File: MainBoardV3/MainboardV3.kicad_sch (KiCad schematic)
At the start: 32 parts, among them J1 Conn_01x02, J10 Conn_01x04, J11 Conn_01x02, J18 Conn_01x03, J19 Conn_02x03_Odd_Even, J2 Conn_01x04, J20 Conn_02x03_Odd_Even, J21 Conn_02x03_Odd_Even, J22 Conn_01x03, J23 Conn_01x05, J24 Conn_02x05_Odd_Even, J3 Conn_01x03, J4 Conn_01x04, J5 Conn_01x05, J7 Conn_01x04, J8 Conn_01x04, J9 Conn_01x04, U2 ESP32-S3-DevKitC

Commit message: Modified to suit needs
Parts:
- removed A1, A2, A3: Pololu_Breakout_DRV8825, Module:Pololu_Breakout-16_15.2x20.3mm, symbol Driver_Motor:Pololu_Breakout_DRV8825
- removed C7, C8, C9: C_Polarized, Capacitor_THT:CP_Radial_D8.0mm_P3.50mm, symbol Device:C_Polarized
- removed J10, J2, J4: Conn_01x04, Connector_Molex:Molex_KK-254_AE-6410-04A_1x04_P2.54mm_Vertical, symbol Connector_Generic:Conn_01x04
- removed J18: Conn_01x03, Connector_PinHeader_2.54mm:PinHeader_1x03_P2.54mm_Vertical, symbol Connector_Generic:Conn_01x03
- removed J19, J20, J21: Conn_02x03_Odd_Even, Connector_PinHeader_2.54mm:PinHeader_2x03_P2.54mm_Vertical, symbol Connector_Generic:Conn_02x03_Odd_Even
- removed J5: Conn_01x05, Connector_JST:JST_XH_B5B-XH-A_1x05_P2.50mm_Vertical, symbol Connector_Generic:Conn_01x05
- removed J7, J8, J9: Conn_01x04, Connector_JST:JST_XH_B4B-XH-A_1x04_P2.50mm_Vertical, symbol Connector_Generic:Conn_01x04
- added C1, C2, C3: C_Polarized, Capacitor_THT:CP_Radial_D8.0mm_P3.50mm, symbol Device:C_Polarized
- added Conn12V1: Conn12V, Connector_AMASS:AMASS_XT30U-F_1x02_P5.0mm_Vertical, symbol Connector_Generic:Conn_01x02
- added Conn5V1: Conn5V, Connector_Molex:Molex_KK-254_AE-6410-02A_1x02_P2.54mm_Vertical, symbol Connector_Generic:Conn_01x02
- added Conn5VL1: Conn5VL, Connector_Molex:Molex_KK-254_AE-6410-02A_1x02_P2.54mm_Vertical, symbol Connector_Generic:Conn_01x02
- added Conn5VP1: Conn5VP, Connector_Molex:Molex_KK-396_A-41791-0002_1x02_P3.96mm_Vertical, symbol Connector_Generic:Conn_01x02
- added ConnAffOled1, ConnAffOled2: ConnAffOled, Connector_JST:JST_EH_B6B-EH-A_1x06_P2.50mm_Vertical, symbol Connector_Generic:Conn_01x06
- added ConnBATT1: ConnBATT, Connector_AMASS:AMASS_XT60-F_1x02_P7.20mm_Vertical, symbol Connector_Generic:Conn_01x02
- added ConnIFM_1: ConnIFM_1, Connector_Molex:Molex_KK-254_AE-6410-03A_1x03_P2.54mm_Vertical, symbol Connector_Generic:Conn_01x03
- added ConnIFM_2: ConnIFM_2, Connector_Molex:Molex_KK-254_AE-6410-03A_1x03_P2.54mm_Vertical, symbol Connector_Generic:Conn_01x03
- added ConnIFM_3: ConnIFM_3, Connector_Molex:Molex_KK-254_AE-6410-03A_1x03_P2.54mm_Vertical, symbol Connector_Generic:Conn_01x03
- added ConnMotor1: ConnMotor1, Connector_JST:JST_EH_B6B-EH-A_1x06_P2.50mm_Vertical, symbol Connector_Generic:Conn_01x06
- added ConnMotor2: ConnMotor2, Connector_JST:JST_EH_B6B-EH-A_1x06_P2.50mm_Vertical, symbol Connector_Generic:Conn_01x06
- added ConnMotor3: ConnMotor3, Connector_JST:JST_EH_B6B-EH-A_1x06_P2.50mm_Vertical, symbol Connector_Generic:Conn_01x06
- added ConnPCA1: Conn_01x06, Connector_JST:JST_EH_B6B-EH-A_1x06_P2.50mm_Vertical, symbol Connector_Generic:Conn_01x06
- added Conn_LIDAR1, Conn_LIDAR2: Conn_LIDAR, Connector_JST:JST_EH_B5B-EH-A_1x05_P2.50mm_Vertical, symbol Connector_Generic:Conn_01x05
- added R10, R6, R8: 470, Resistor_SMD:R_1206_3216Metric_Pad1.30x1.75mm_HandSolder, symbol Device:R_Small
- added R11, R7, R9: 110, Resistor_SMD:R_1206_3216Metric_Pad1.30x1.75mm_HandSolder, symbol Device:R_Small
- Tir.1: footprint Connector_JST:JST_XH_B2B-XH-A_1x02_P2.50mm_Vertical -> Connector_Molex:Molex_KK-254_AE-6410-02A_1x02_P2.54mm_Vertical
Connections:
- net +12V: now also Conn12V1.2 (Pin_2), ConnIFM_1.2 (Pin_2), ConnIFM_2.2 (Pin_2), ConnIFM_3.2 (Pin_2)
- net +3.3V: no longer U2.1 (3V3), U2.2 (3V3)
- net +5V: now also Conn5V1.1 (Pin_1), ConnPCA1.5 (Pin_5)
- net +5VP: now also Conn5VP1.1 (Pin_1), ConnPCA1.6 (Pin_6)
- net DIR1: now also ConnMotor1.6 (Pin_6)
- net DIR2: now also ConnMotor2.6 (Pin_6)
- net DIR3: now also ConnMotor3.6 (Pin_6)
- net EN: now also ConnMotor2.4 (Pin_4), ConnMotor3.4 (Pin_4)
- net GND: now also C1.2, C2.2, C3.2, Conn12V1.1 (Pin_1), Conn5V1.2 (Pin_2), Conn5VL1.2 (Pin_2), Conn5VP1.2 (Pin_2), ConnAffOled1.1 (Pin_1), ConnAffOled1.3 (Pin_3), ConnAffOled2.1 (Pin_1), ConnAffOled2.3 (Pin_3), ConnBATT1.1 (Pin_1), ConnIFM_1.3 (Pin_3), ConnIFM_2.3 (Pin_3), ConnIFM_3.3 (Pin_3), ConnMotor1.2 (Pin_2), ConnMotor2.2 (Pin_2), ConnMotor3.2 (Pin_2), ConnPCA1.1 (Pin_1), Conn_LIDAR1.2 (Pin_2), Conn_LIDAR2.2 (Pin_2), R11.2, R7.2, R9.2
- net LIDARRX: now also Conn_LIDAR1.3 (Pin_3), Conn_LIDAR2.3 (Pin_3)
- net LIDARTX: now also Conn_LIDAR1.4 (Pin_4), Conn_LIDAR2.4 (Pin_4)
- net PWMLIDAR: now also Conn_LIDAR1.1 (Pin_1), Conn_LIDAR2.1 (Pin_1)
- net SCL: now also ConnAffOled1.4 (Pin_4), ConnAffOled2.4 (Pin_4), ConnPCA1.3 (Pin_3)
- net SDA: now also ConnAffOled1.5 (Pin_5), ConnAffOled2.5 (Pin_5), ConnPCA1.4 (Pin_4)
- net STEP1: now also ConnMotor1.5 (Pin_5)
- net STEP2: now also ConnMotor2.5 (Pin_5)
- net STEP3: now also ConnMotor3.5 (Pin_5)
- new net: U2.1 (3V3), U2.2 (3V3)
- new net: ConnIFM_3.1 (Pin_1), R10.1
- new net: ConnIFM_1.1 (Pin_1), R6.1
- new net: ConnIFM_2.1 (Pin_1), R8.1
- new net +5VL: Conn5VL1.1 (Pin_1), ConnAffOled1.2 (Pin_2), ConnAffOled2.2 (Pin_2), Conn_LIDAR1.5 (Pin_5), Conn_LIDAR2.5 (Pin_5)
- new net +BATT: C1.1, C2.1, C3.1, ConnBATT1.2 (Pin_2), ConnMotor1.1 (Pin_1), ConnMotor2.1 (Pin_1), ConnMotor3.1 (Pin_1)
- new net ENA_STEPPERS: ConnMotor1.4 (Pin_4)
- new net IFM1: R6.2, R7.1
- new net IFM2: R8.2, R9.1
- new net IFM3: R10.2, R11.1
- new net RESET_OLED: ConnAffOled1.6 (Pin_6), ConnAffOled2.6 (Pin_6)
- new net SERVO_ENABLE: ConnPCA1.2 (Pin_2)
- no-connect marks 8 -> 5
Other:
- note added: "Alimentation 5V Logique"
- note added: "Alimentation 5V Puissance"
- note added: "Vout = 2,276V"
- moved on the sheet: H4, U5

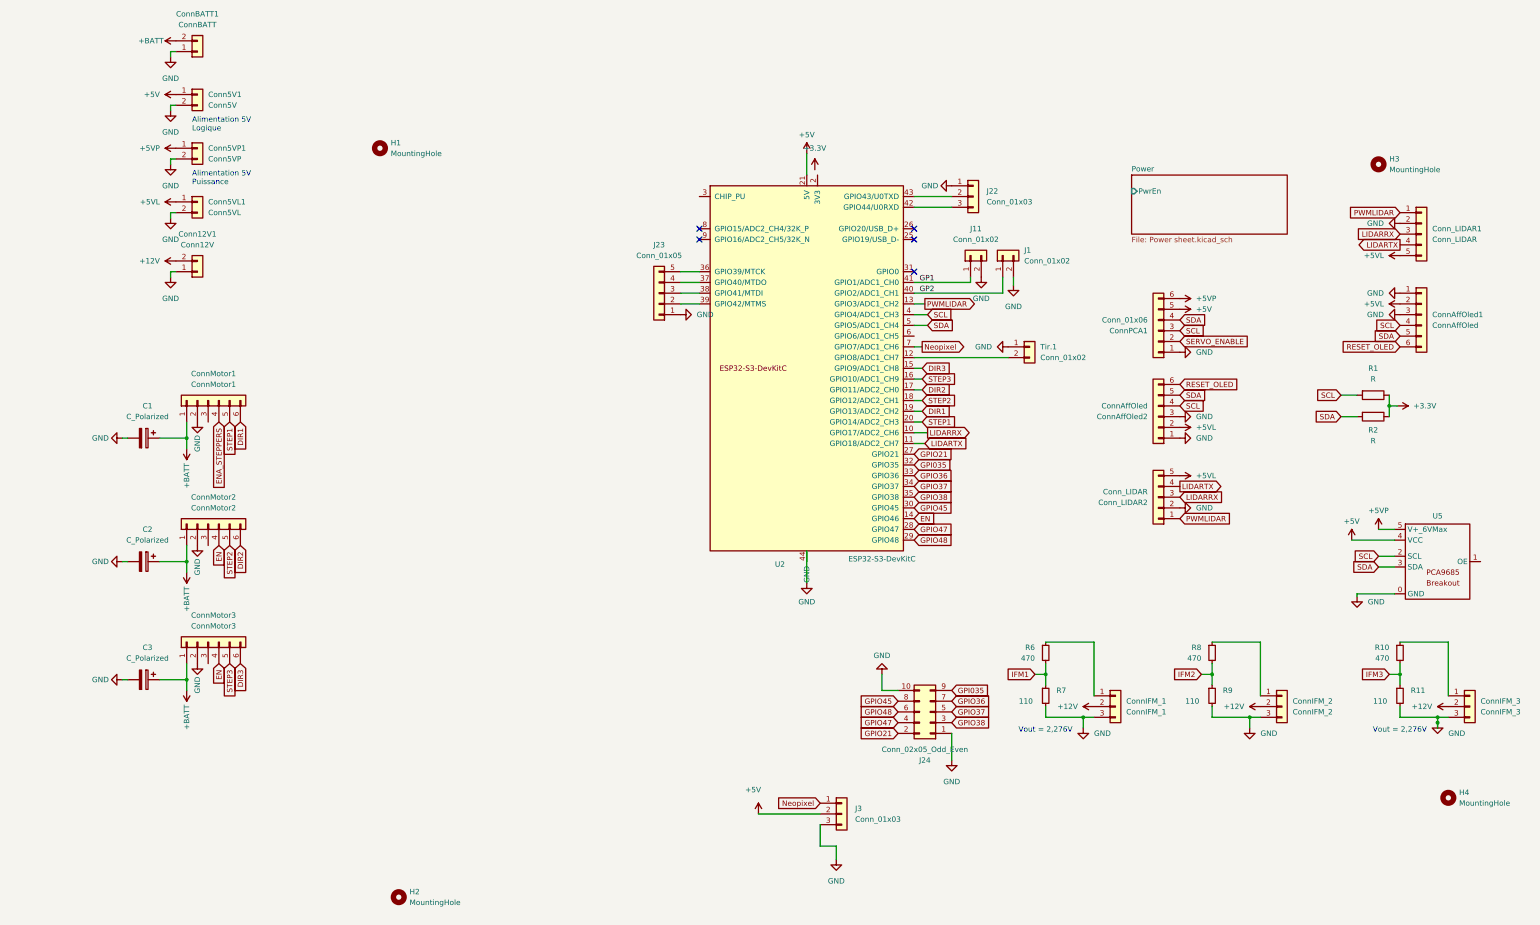
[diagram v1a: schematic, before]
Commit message: Adapted schematic to existing needs
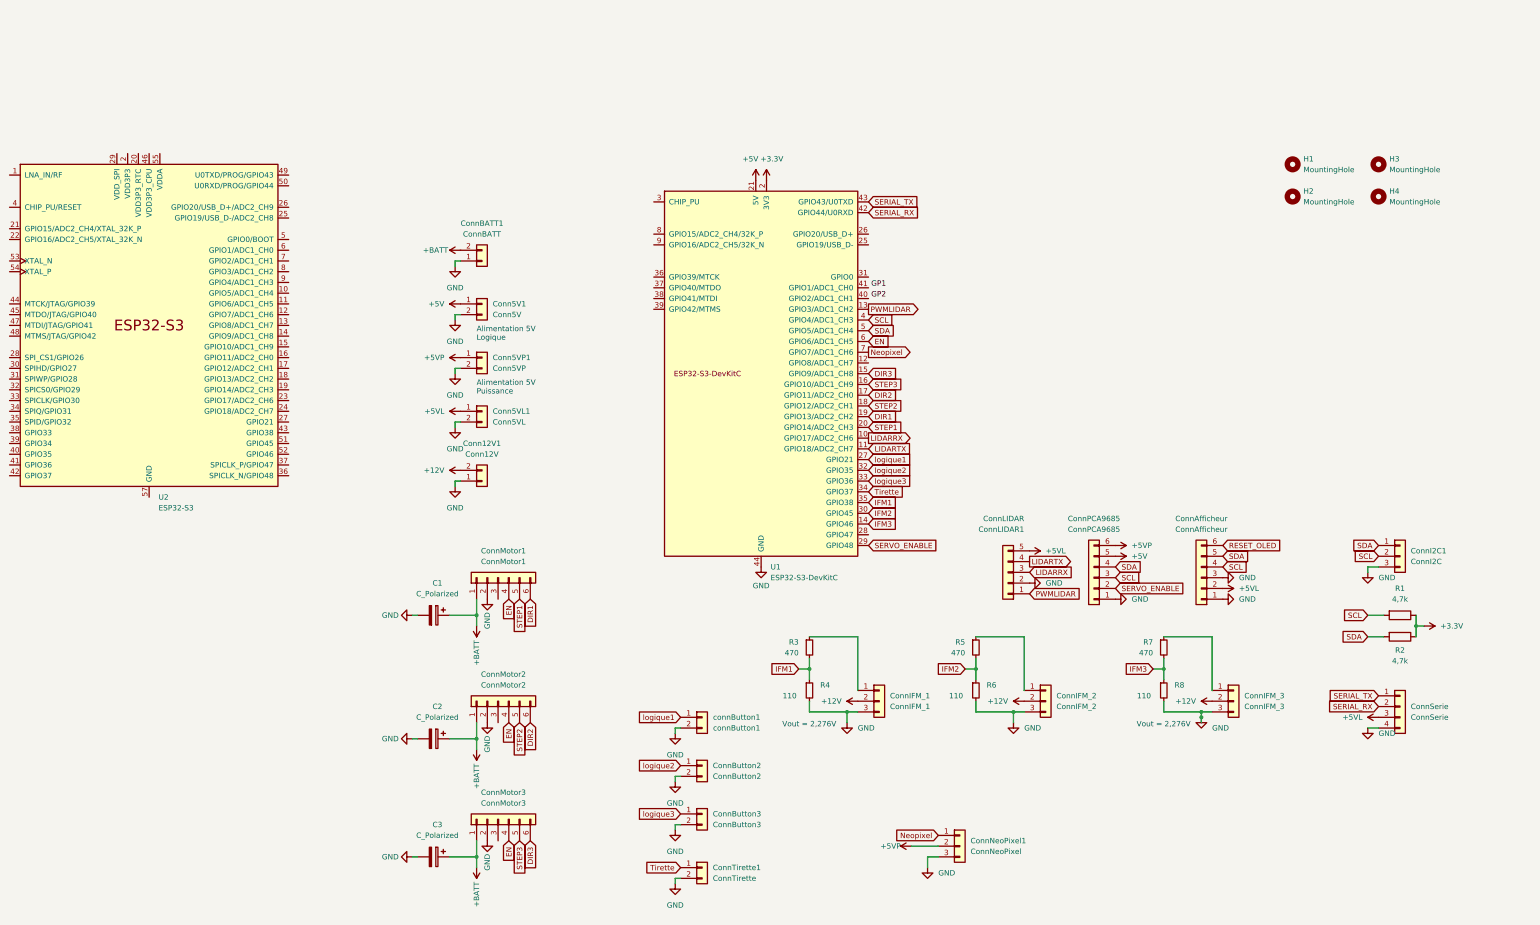
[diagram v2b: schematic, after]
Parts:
- removed ConnAffOled1: ConnAffOled, Connector_JST:JST_EH_B6B-EH-A_1x06_P2.50mm_Vertical, symbol Connector_Generic:Conn_01x06
- removed Conn_LIDAR1: Conn_LIDAR, Connector_JST:JST_EH_B5B-EH-A_1x05_P2.50mm_Vertical, symbol Connector_Generic:Conn_01x05
- removed J1, J11: Conn_01x02, Connector_JST:JST_XH_B2B-XH-A_1x02_P2.50mm_Vertical, symbol Connector_Generic:Conn_01x02
- removed J22, J3: Conn_01x03, Connector_PinHeader_2.54mm:PinHeader_1x03_P2.54mm_Vertical, symbol Connector_Generic:Conn_01x03
- removed J23: Conn_01x05, Connector_JST:JST_XH_B5B-XH-A_1x05_P2.50mm_Vertical, symbol Connector_Generic:Conn_01x05
- removed J24: Conn_02x05_Odd_Even, Connector_IDC:IDC-Header_2x05_P2.54mm_Vertical, symbol Connector_Generic:Conn_02x05_Odd_Even
- removed Tir.1: Conn_01x02, Connector_Molex:Molex_KK-254_AE-6410-02A_1x02_P2.54mm_Vertical, symbol Connector_Generic:Conn_01x02
- removed U2: ESP32-S3-DevKitC, ESP:ESP32-S3-DevKitC, symbol ESP32:ESP32-S3-DevKitC
- removed U5: ~, Custom:PCA9685breakout, symbol PCM:PWMI2C
- added ConnButton2: ConnButton2, Connector_Molex:Molex_KK-254_AE-6410-02A_1x02_P2.54mm_Vertical, symbol Connector_Generic:Conn_01x02
- added ConnButton3: ConnButton3, Connector_Molex:Molex_KK-254_AE-6410-02A_1x02_P2.54mm_Vertical, symbol Connector_Generic:Conn_01x02
- added ConnI2C1: ConnI2C, Connector_Molex:Molex_KK-254_AE-6410-03A_1x03_P2.54mm_Vertical, symbol Connector_Generic:Conn_01x03
- added ConnNeoPixel1: ConnNeoPixel, Connector_Molex:Molex_KK-254_AE-6410-03A_1x03_P2.54mm_Vertical, symbol Connector_Generic:Conn_01x03
- added ConnSerie: ConnSerie, Connector_JST:JST_EH_B4B-EH-A_1x04_P2.50mm_Vertical, symbol Connector_Generic:Conn_01x04
- added ConnTirette1: ConnTirette, Connector_Molex:Molex_KK-254_AE-6410-02A_1x02_P2.54mm_Vertical, symbol Connector_Generic:Conn_01x02
- added U1: ESP32-S3-DevKitC, PCM_Espressif:ESP32-S3-DevKitC, symbol PCM_Espressif:ESP32-S3-DevKitC
- added U2: ESP32-S3, Package_DFN_QFN:QFN-56-1EP_7x7mm_P0.4mm_EP5.6x5.6mm, symbol PCM_Espressif:ESP32-S3
- added connButton1: connButton1, Connector_Molex:Molex_KK-254_AE-6410-02A_1x02_P2.54mm_Vertical, symbol Connector_Generic:Conn_01x02
- ConnAfficheur: renamed from ConnAffOled2; value ConnAffOled -> ConnAfficheur
- ConnLIDAR1: renamed from Conn_LIDAR2; value Conn_LIDAR -> ConnLIDAR
- ConnPCA9685: renamed from ConnPCA1; value Conn_01x06 -> ConnPCA9685
- R1, R2: value R -> 4,7k
- renumbered R6 to R3, R7 to R4, R8 to R5, R9 to R6, R10 to R7, R11 to R8
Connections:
- net ENA_STEPPERS is gone; now on net EN: ConnMotor1.4 (Pin_4)
- net +3.3V: now also U1.1 (3V3), U1.2 (3V3)
- net +5V: now also U1.21 (5V)
- net +5VL: now also ConnSerie.3 (Pin_3)
- net +5VP: now also ConnNeoPixel1.2 (Pin_2)
- net DIR1: now also U1.19 (GPIO13/ADC2_CH2)
- net DIR2: now also U1.17 (GPIO11/ADC2_CH0)
- net DIR3: now also U1.15 (GPIO9/ADC1_CH8)
- net EN: now also U1.6 (GPIO6/ADC1_CH5)
- net GND: now also ConnButton2.2 (Pin_2), ConnButton3.2 (Pin_2), ConnI2C1.3 (Pin_3), ConnNeoPixel1.3 (Pin_3), ConnSerie.4 (Pin_4), ConnTirette1.2 (Pin_2), U1.22 (GND), U1.23 (GND), U1.24 (GND), U1.44 (GND), connButton1.2 (Pin_2)
- net IFM1: now also U1.35 (GPIO38)
- net IFM2: now also U1.30 (GPIO45)
- net IFM3: now also U1.14 (GPIO46)
- net LIDARRX: now also U1.10 (GPIO17/ADC2_CH6)
- net LIDARTX: now also U1.11 (GPIO18/ADC2_CH7)
- net Neopixel: now also ConnNeoPixel1.1 (Pin_1), U1.7 (GPIO7/ADC1_CH6)
- net PWMLIDAR: now also U1.13 (GPIO3/ADC1_CH2)
- net SCL: now also ConnI2C1.2 (Pin_2), U1.4 (GPIO4/ADC1_CH3)
- net SDA: now also ConnI2C1.1 (Pin_1), U1.5 (GPIO5/ADC1_CH4)
- net SERVO_ENABLE: now also U1.29 (GPIO48)
- net STEP1: now also U1.20 (GPIO14/ADC2_CH3)
- net STEP2: now also U1.18 (GPIO12/ADC2_CH1)
- net STEP3: now also U1.16 (GPIO10/ADC1_CH9)
- new net: U2.55 (VDDA), U2.56 (VDDA)
- new net SERIAL_RX: ConnSerie.2 (Pin_2), U1.42 (GPIO44/U0RXD)
- new net SERIAL_TX: ConnSerie.1 (Pin_1), U1.43 (GPIO43/U0TXD)
- new net Tirette: ConnTirette1.1 (Pin_1), U1.34 (GPIO37)
- new net VDD3P3: U2.2 (VDD3P3), U2.3 (VDD3P3)
- new net logique1: U1.27 (GPIO21), connButton1.1 (Pin_1)
- new net logique2: ConnButton2.1 (Pin_1), U1.32 (GPIO35)
- new net logique3: ConnButton3.1 (Pin_1), U1.33 (GPIO36)
- no-connect marks 5 -> 0
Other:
- removed sheet Power
- moved on the sheet: C1, C2, C3, Conn12V1, Conn5V1, Conn5VL1, Conn5VP1, ConnAfficheur, ConnBATT1, ConnIFM_1, ConnIFM_2, ConnIFM_3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
